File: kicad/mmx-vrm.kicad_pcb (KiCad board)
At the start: 2 copper layers, 39.4 x 44.2 mm, 30 parts, among them J1 Conn_02x15_Row_Letter_First, Q1 Q_NMOS_GDS, Q2 Q_NMOS_GDS, Q3 Q_NPN_BEC, SW1 SW_DIP_x04, U1 NCP1579

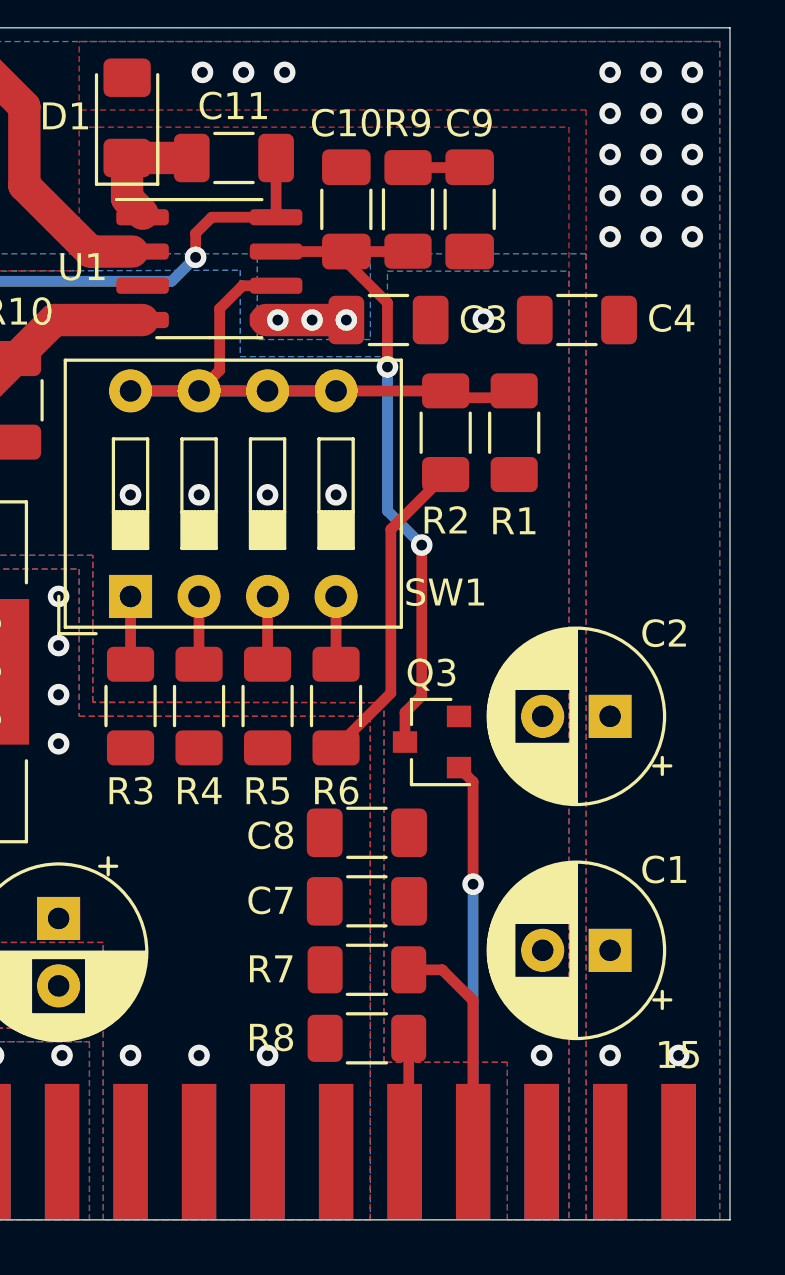
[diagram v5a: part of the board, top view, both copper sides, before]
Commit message: Switched to KiCad 7
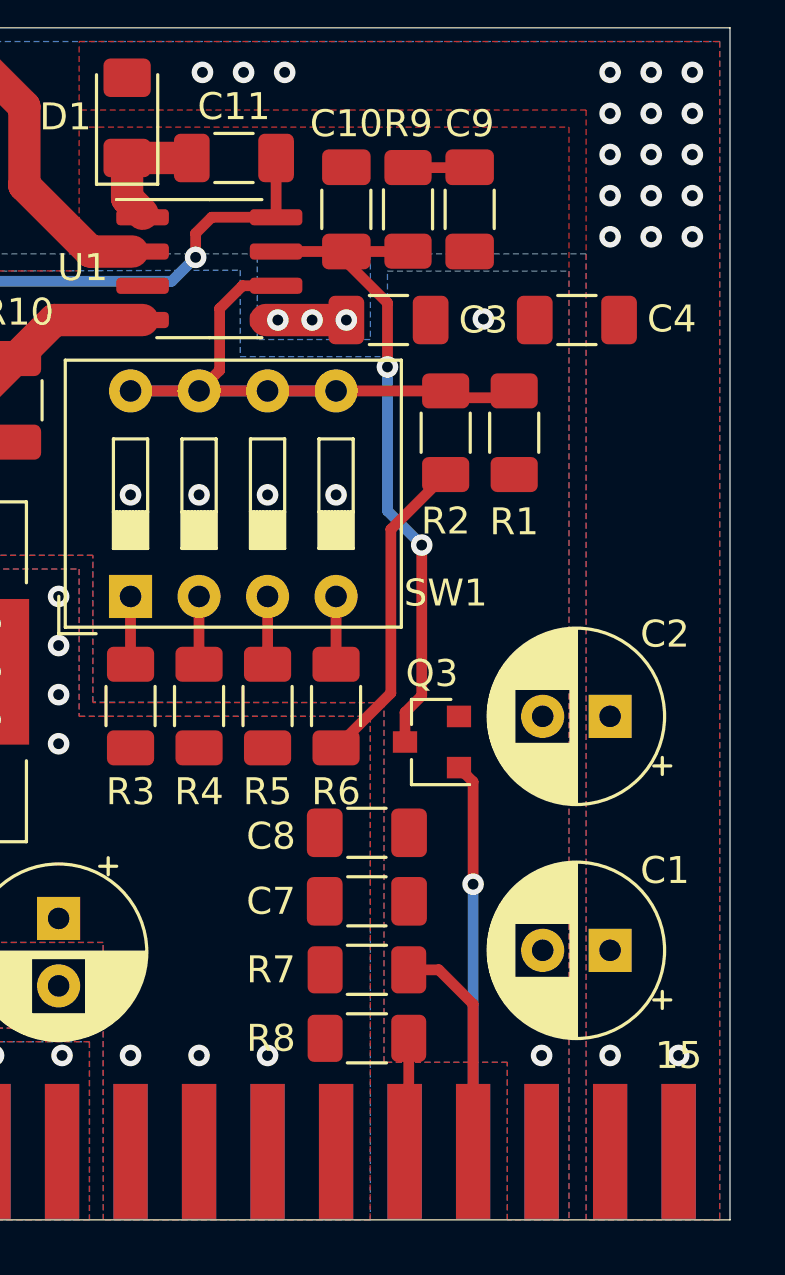
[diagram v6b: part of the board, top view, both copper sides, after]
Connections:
- J1 pad a3: (no net) -> +12V
- J1 pad a9: (no net) -> unconnected-(J1-Pin_a9-Pada9)
- J1 pad b11: (no net) -> unconnected-(J1-Pin_b11-Padb11)
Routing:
- net Net-(R6-Pad2): track 3.02 -> 2.51 mm
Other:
- net class Default removed
- net class Power removed

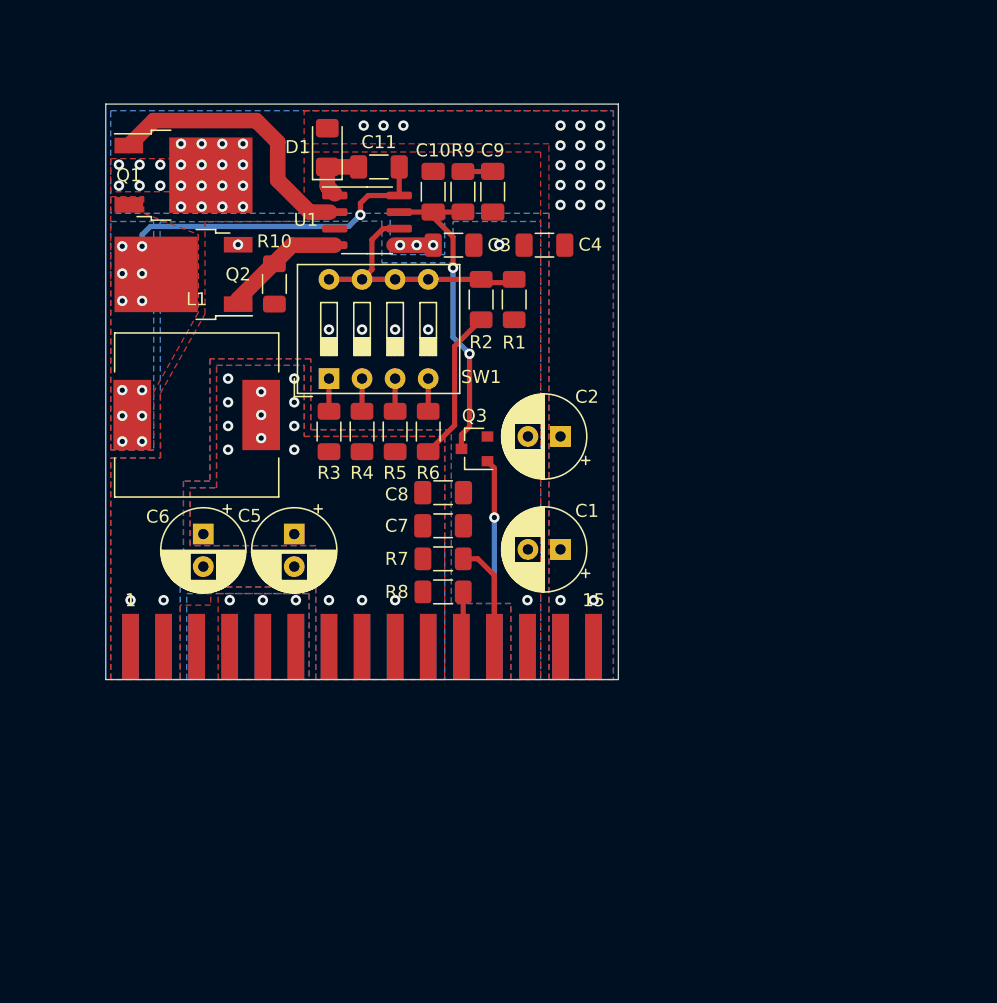
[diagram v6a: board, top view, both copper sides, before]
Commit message: Wide version
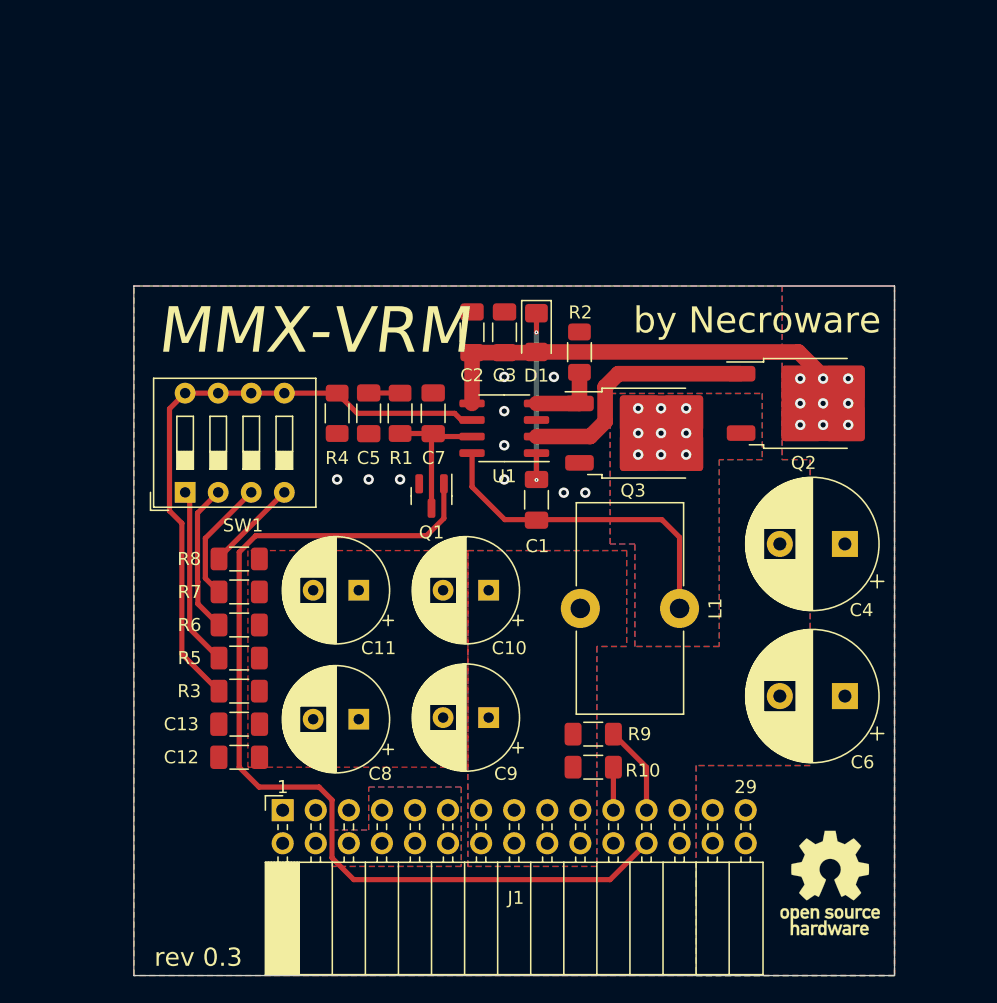
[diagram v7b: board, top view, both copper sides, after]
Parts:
- removed the REF** at (151.9, 78.6)
- added C12: 4.7u, Capacitor_SMD:C_1206_3216Metric_Pad1.33x1.80mm_HandSolder, F.Cu at (129.0, 115.2)
- added C13: 0.1u, Capacitor_SMD:C_1206_3216Metric_Pad1.33x1.80mm_HandSolder, F.Cu at (129.0, 112.6)
- added REF**: OSHW-Logo_7.5x8mm_SilkScreen, Symbol:OSHW-Logo_7.5x8mm_SilkScreen, F.Cu at (174.4, 124.8)
- C1: value 1mF -> 0.1u; footprint Capacitor_THT:CP_Radial_D6.3mm_P2.50mm -> Capacitor_SMD:C_1206_3216Metric_Pad1.33x1.80mm_HandSolder
- C10: value 386p -> 1000u; footprint Capacitor_SMD:C_1206_3216Metric_Pad1.33x1.80mm_HandSolder -> Capacitor_THT:CP_Radial_D8.0mm_P3.50mm
- C11, C8: value 0.1u -> 1000u; footprint Capacitor_SMD:C_1206_3216Metric_Pad1.33x1.80mm_HandSolder -> Capacitor_THT:CP_Radial_D8.0mm_P3.50mm
- C2: value 1mF -> 4.7u; footprint Capacitor_THT:CP_Radial_D6.3mm_P2.50mm -> Capacitor_SMD:C_1206_3216Metric_Pad1.33x1.80mm_HandSolder
- C4: value 4.7u -> 3300u; footprint Capacitor_SMD:C_1206_3216Metric_Pad1.33x1.80mm_HandSolder -> Capacitor_THT:CP_Radial_D10.0mm_P5.00mm
- C5: value 1mF -> 22n; footprint Capacitor_THT:CP_Radial_D6.3mm_P2.50mm -> Capacitor_SMD:C_1206_3216Metric_Pad1.33x1.80mm_HandSolder
- C6: value 1mF -> 3300u; footprint Capacitor_THT:CP_Radial_D6.3mm_P2.50mm -> Capacitor_THT:CP_Radial_D10.0mm_P5.00mm
- C7: value 4.7u -> 220p
- C9: value 81n -> 1000u; footprint Capacitor_SMD:C_1206_3216Metric_Pad1.33x1.80mm_HandSolder -> Capacitor_THT:CP_Radial_D8.0mm_P3.50mm
- J1: footprint mmx-vrm:EDGE_30-pin -> Connector_PinSocket_2.54mm:PinSocket_2x15_P2.54mm_Horizontal
- L1: value 1,2uH -> 2,5uH; footprint Inductor_SMD:L_12x12mm_H4.5mm -> Inductor_THT:L_Toroid_Vertical_L16.0mm_W8.0mm_P7.62mm
- Q1: value Q_NMOS_GDS -> Q_NPN_BEC; footprint Package_TO_SOT_SMD:TO-252-2 -> Package_TO_SOT_SMD:SOT-23
- Q3: value Q_NPN_BEC -> Q_NMOS_GDS; footprint Package_TO_SOT_SMD:SOT-23 -> Package_TO_SOT_SMD:TO-252-2
- R1: value 1K -> 6,3K
- R10, R4: value 15K -> 1K
- R2, R6: value 3K -> 15K
- R3: value 21K -> 3K
- R5: value 6,3K -> 21K
- R7: value 0 -> 6,3K
- R8: value 1K -> 3K
- R9: value 3K -> 0
- moved C6 50.8 mm to (175.5, 110.5), turned to 180 degrees
- moved Q2 48.9 mm to (172.6, 88.0), turned to 0 degrees
- moved R10 44.5 mm to (156.2, 116.0), turned to 180 degrees
- moved R9 42.8 mm to (156.2, 113.4), turned to 180 degrees
- moved C9 40.4 mm to (148.2, 112.1), turned to 180 degrees
- moved L1 40.0 mm to (162.8, 103.8), turned to -90 degrees
- moved C11 32.5 mm to (138.2, 102.4), turned to 180 degrees
- moved C4 32.5 mm to (175.5, 98.8)
- moved Q1 31.1 mm to (143.8, 95.1), turned to -90 degrees
- moved C10 30.9 mm to (148.2, 102.4), turned to 180 degrees
- moved D1 21.4 mm to (151.8, 82.6), turned to -90 degrees
- moved R5 21.1 mm to (129.0, 107.6), turned to 180 degrees
- moved R3 21.1 mm to (129.0, 110.1), turned to 180 degrees
- moved R6 20.8 mm to (129.0, 105.0), turned to 180 degrees
- moved U1 19.1 mm to (149.4, 89.9), turned to 180 degrees
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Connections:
- C1 pad 1: +5V -> /BST
- C1 pad 2: GND -> /PHASE
- C10 pad 1: Net-(Q3-C) -> VCORE
- C11 pad 1: Net-(D1-K) -> VCORE
- C11 pad 2: Net-(Q1-S) -> GND
- C5 pad 1: VCORE -> Net-(C5-Pad1)
- C6 pad 1: VCORE -> +5V
- C7 pad 1: VCORE -> /COMP
- C9 pad 1: Net-(C9-Pad1) -> VCORE
- D1 pad 1: Net-(D1-K) -> /BST
- L1 pad 1: Net-(Q1-S) -> /PHASE
- Q1 pad 1: Net-(Q1-G) -> DISABLE
- Q1 pad 2: +5V -> GND
- Q1 pad 3: Net-(Q1-S) -> /COMP
- Q2 pad 1: Net-(Q2-G) -> /TG
- Q2 pad 2: Net-(Q1-S) -> +5V
- Q2 pad 3: GND -> /PHASE
- Q3 pad 1: DISABLE -> /BG
- Q3 pad 2: GND -> /PHASE
- Q3 pad 3: Net-(Q3-C) -> GND
- R1 pad 1: FB -> /COMP
- R1 pad 2: GND -> Net-(C5-Pad1)
- R10 pad 1: GND -> PWRGOOD
- R10 pad 2: Net-(Q2-G) -> VCORE
- R2 pad 1: VCORE -> GND
- R2 pad 2: FB -> /BG
- R3 pad 2: Net-(R3-Pad2) -> FB
- R4 pad 1: VCORE -> FB
- R4 pad 2: Net-(R4-Pad2) -> GND
- R7 pad 1: SENSE -> VCORE
- R7 pad 2: VCORE -> Net-(R7-Pad2)
- R8 pad 1: PWRGOOD -> VCORE
- R8 pad 2: VCORE -> Net-(R8-Pad2)
- R9 pad 1: Net-(Q3-C) -> SENSE
- R9 pad 2: Net-(C9-Pad1) -> VCORE
- SW1 pad 1: Net-(R3-Pad2) -> Net-(R5-Pad2)
- SW1 pad 2: Net-(R4-Pad2) -> Net-(R6-Pad2)
- SW1 pad 3: Net-(R5-Pad2) -> Net-(R7-Pad2)
- SW1 pad 4: Net-(R6-Pad2) -> Net-(R8-Pad2)
- U1 pad 1: Net-(D1-K) -> /BST
- U1 pad 2: Net-(Q1-G) -> /TG
- U1 pad 4: Net-(Q2-G) -> /BG
- U1 pad 7: Net-(Q3-C) -> /COMP
- U1 pad 8: Net-(Q1-S) -> /PHASE
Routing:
- net DISABLE: track 13.2 -> 74.6 mm, vias 1 -> 0
- net +5V: track 2.31 -> 33.7 mm, vias 45 -> 9
- net /PHASE: track 0.00 -> 25.6 mm, vias 0 -> 9
- net Net-(Q3-C): track 24.6 -> 0.00 mm, vias 2 -> 0
- net Net-(Q1-S): track 24.2 -> 0.00 mm, vias 13 -> 0
- net Net-(Q1-G): track 20.9 -> 0.00 mm
- net FB: track 27.7 -> 47.8 mm
- net /TG: track 0.00 -> 19.3 mm
- net /BST: track 0.00 -> 14.8 mm, vias 0 -> 2
- net VCORE: track 11.8 -> 0.00 mm, vias 14 -> 0
- net /COMP: track 0.00 -> 11.4 mm
- net Net-(R5-Pad2): track 2.51 -> 13.8 mm
- net Net-(R7-Pad2): track 0.00 -> 9.54 mm
- net Net-(Q2-G): track 9.52 -> 0.00 mm
- net Net-(R6-Pad2): track 2.51 -> 11.5 mm
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- added copper zone on B.Cu, net /PHASE
- added copper zone on F.Cu, net /PHASE
- removed copper zone on B.Cu, net Net-(Q1-S)
- removed copper zone on F.Cu, net Net-(Q1-S)
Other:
- board size 39.4 x 44.2 mm -> 58.4 x 53 mm
- board text added: "29"
- board text added: "MMX-VRM"
- board text added: "SW1 Settings: 3.2V: 0000 | 2.1V: 1110 2.9V: 1000 | 2.0V: 0001 2.8V: 0100 | 1.9V: 1001 2.6V: 1100 | 1.8V: 1101 2.4V: 0010 | 1.7V: 0111 2.3V: 1010 | 1.6V: 1111 2.2V: 0110 |"
- board text added: "by Necroware"
- board text added: "rev ${REVISION}"
- board text added: "youtube.com/@necro_ware github.com/necroware"
- board text removed: "15"
- board text removed: "MMX-VRM by Necroware"
- board text removed: "SW1 Settings: 0000: 3.2V 1000: 2.9V 0100: 2.8V 1100: 2.6V 0010: 2.4V 1010: 2.3V 0110: 2.2V 1110: 2.1V 0001: 2.0V 1001: 1.9V 1101: 1.8V 0111: 1.7V 1111: 1.6V"
- board text removed: "rev 0.3"

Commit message: Updated parameters
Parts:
- R1: value 6,3K -> 15K
